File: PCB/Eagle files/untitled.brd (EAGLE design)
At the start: 57 x 27 mm, 38 parts, among them U1 AMS1117-3.3, U2 AMS1117-1.2, U3 ICE40UP3K-UWG30ITR50, U4 AT25SF041

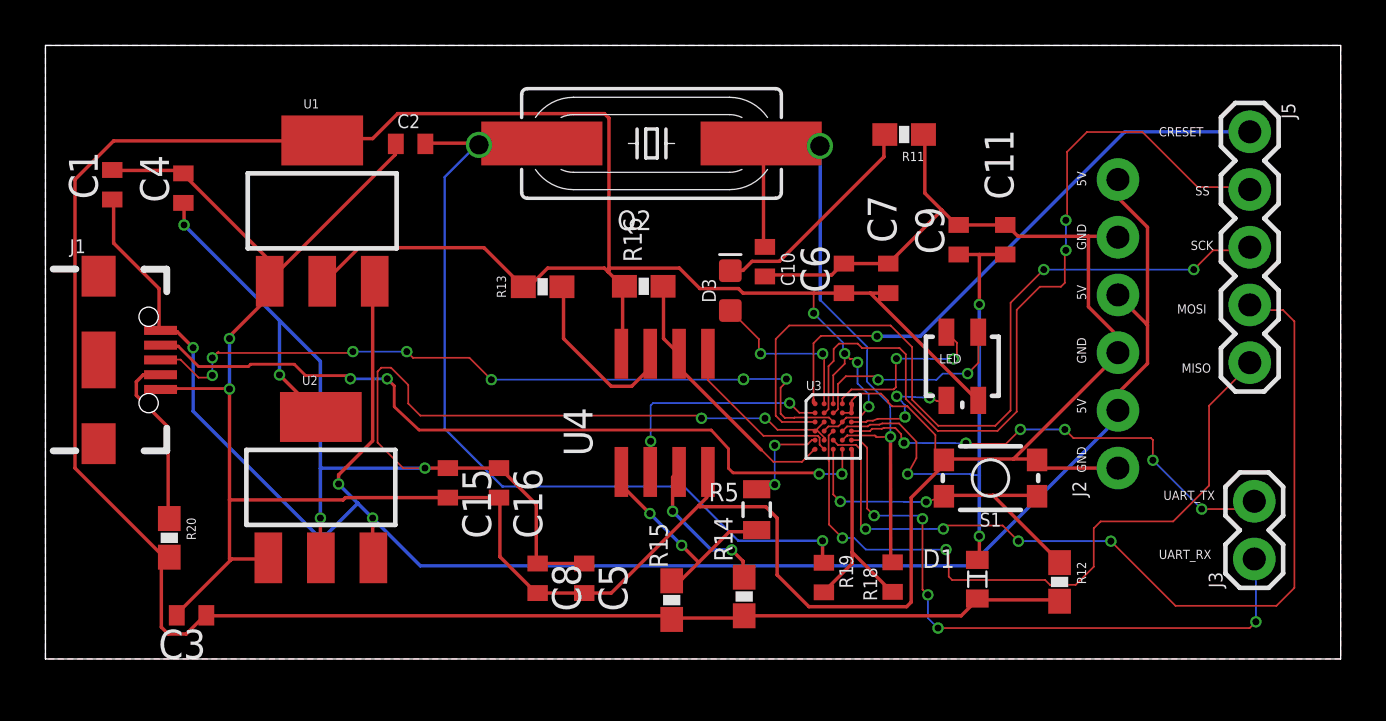
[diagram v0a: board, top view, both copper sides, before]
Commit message: trace width update
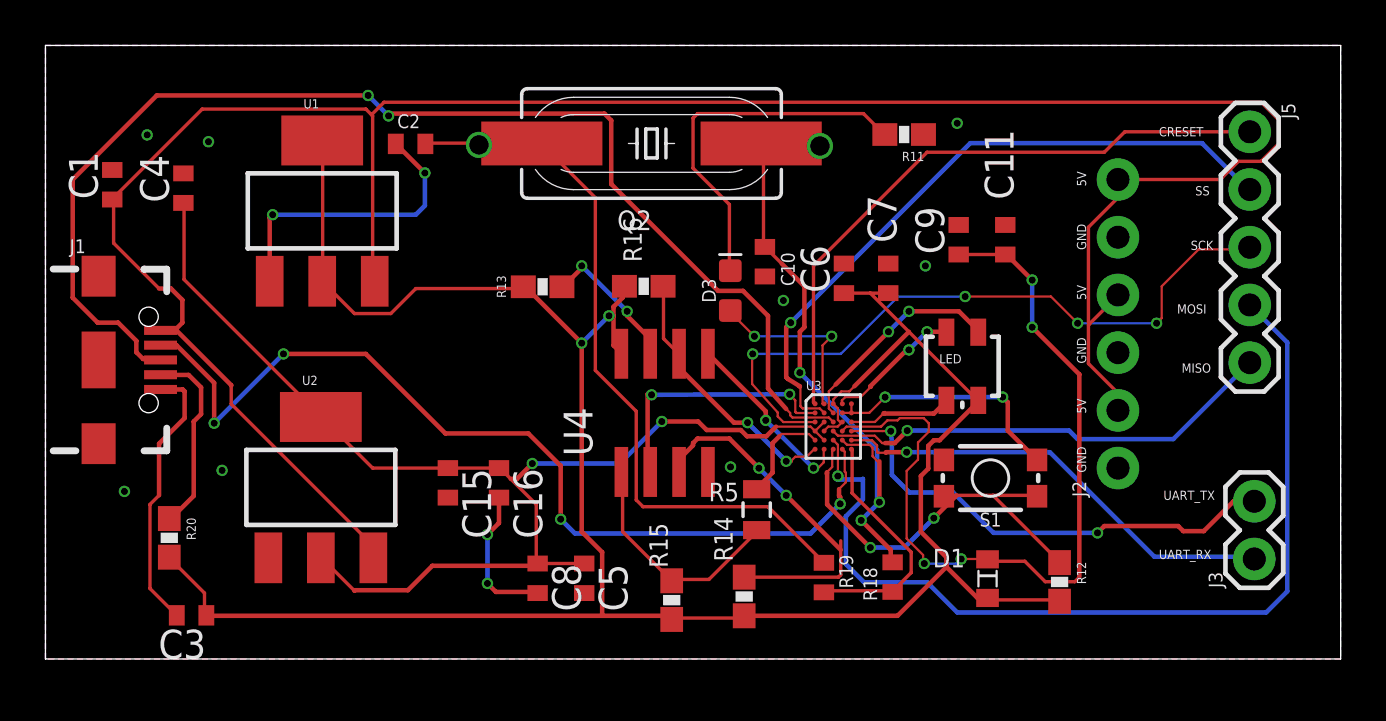
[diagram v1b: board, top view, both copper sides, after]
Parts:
- moved D1 0.45 mm to (41.5, 3.79)
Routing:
- net GND: track 134.2 -> 42.8 mm, vias 2 -> 14
- net +3.3V: track 142.7 -> 105.1 mm, vias 4 -> 2
- net D+: track 33.9 -> 55.1 mm, vias 8 -> 2
- net 5V: track 84.5 -> 104.8 mm, vias 3 -> 0
- net N$18: track 24.0 -> 36.8 mm, vias 3 -> 4
- net 1.2V: track 66.0 -> 54.4 mm, vias 6 -> 2
- net MISO: track 31.7 -> 20.3 mm, vias 2 -> 1
- net N$6: track 6.63 -> 16.5 mm
- net UART_RX: track 28.1 -> 20.1 mm, vias 6 -> 1
- net SS: track 36.6 -> 29.7 mm, vias 2 -> 1
- net D-: track 34.6 -> 41.4 mm
- net N$13: track 9.82 -> 16.3 mm
- net N$24: track 38.1 -> 32.0 mm, vias 1 -> 0
- net SCK: track 35.5 -> 30.6 mm, vias 2 -> 4
- net CRESETB: track 15.3 -> 18.4 mm
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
